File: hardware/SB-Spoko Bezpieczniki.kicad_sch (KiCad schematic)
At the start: 17 parts, among them IC1 STM32L4P5RET6, SW1 RESET, Y1 THE_CLOCK

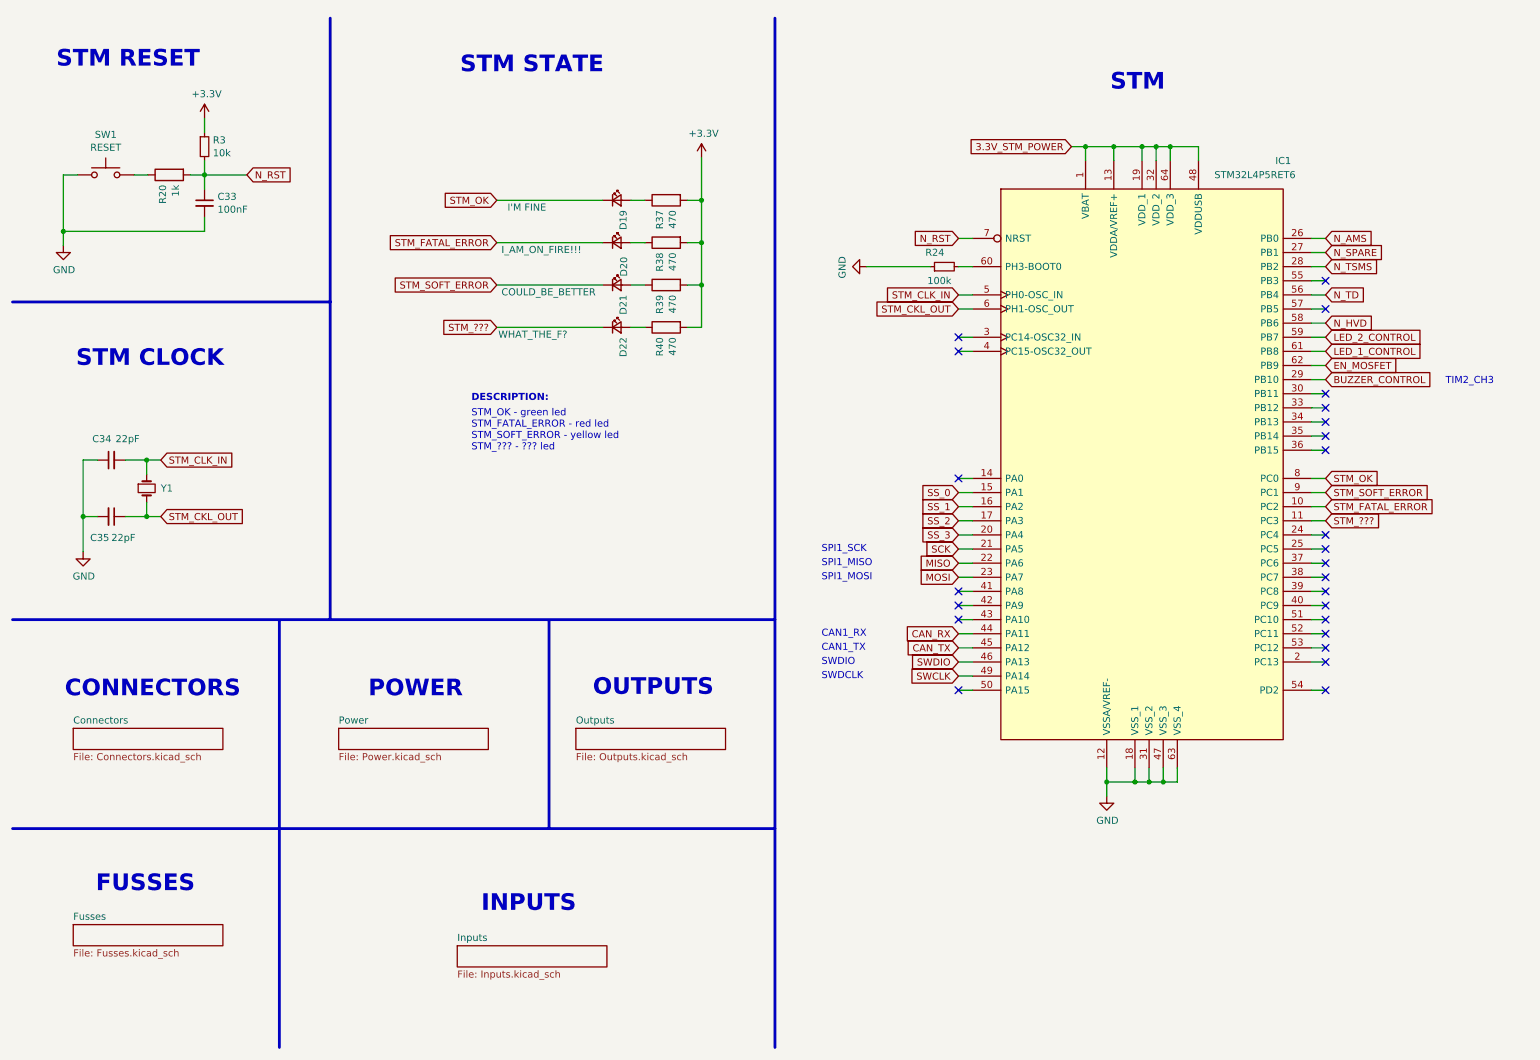
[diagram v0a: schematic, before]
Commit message: changed clock and 5v converter coils, footprints rearrange commponets to fit the need now the board connector is vertical not horizontal relative to the pcb's longest side
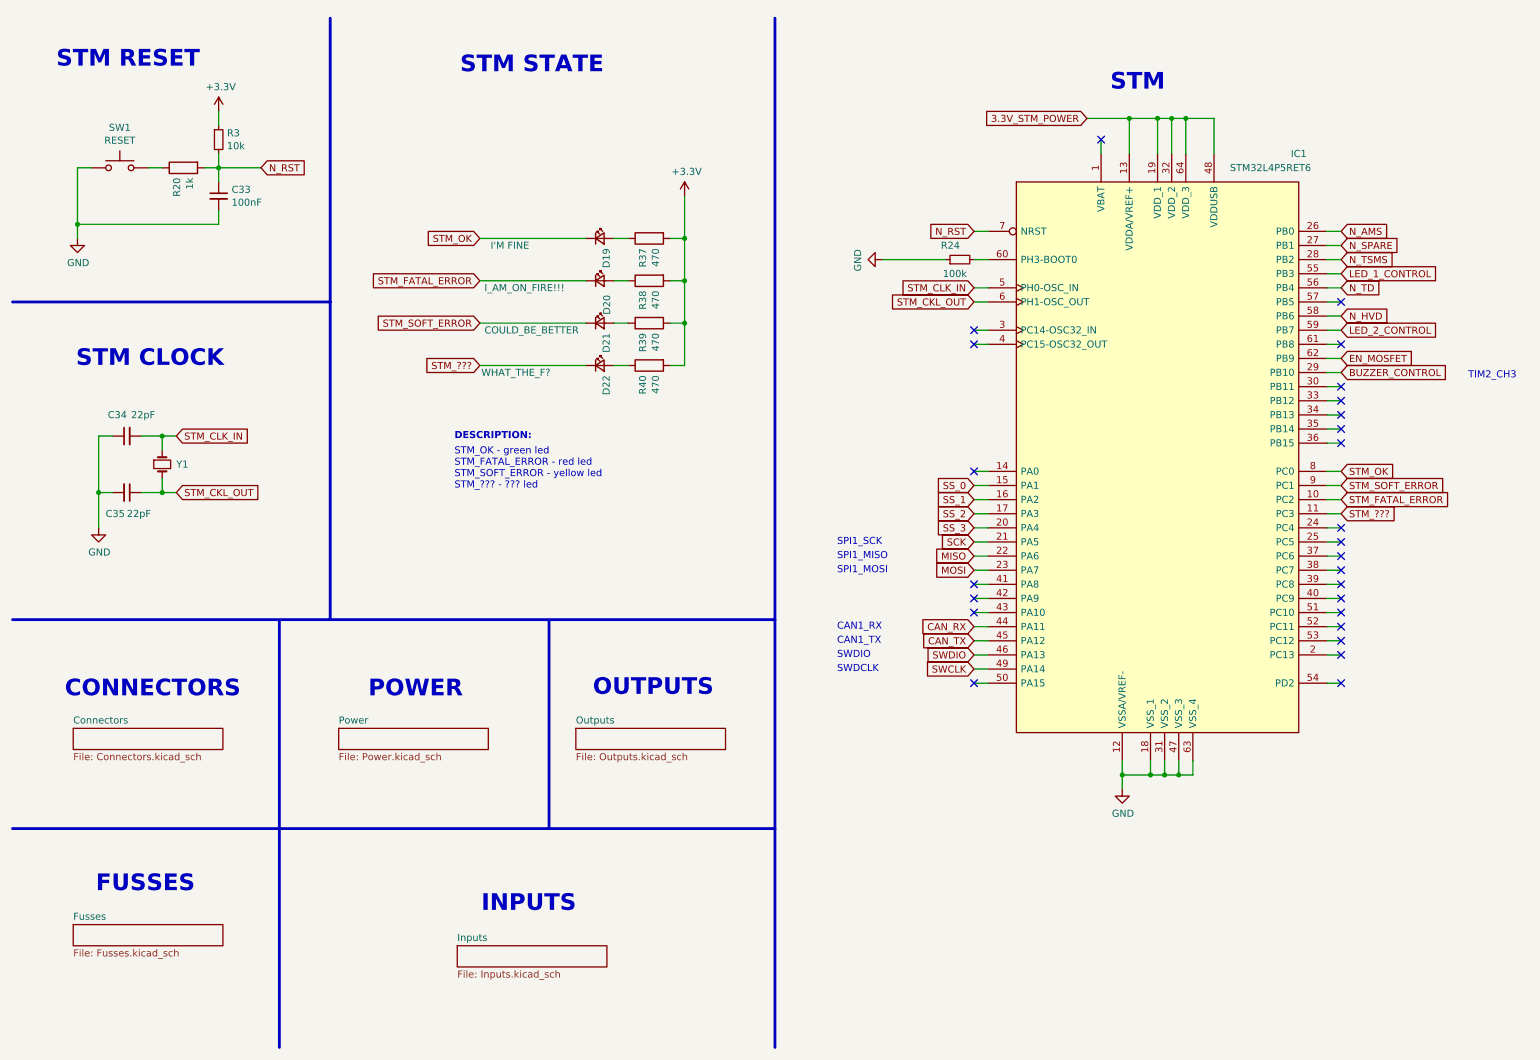
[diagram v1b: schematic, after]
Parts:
- Y1: footprint Crystal:Crystal_SMD_HC49-SD -> Crystal:Crystal_SMD_3225-4Pin_3.2x2.5mm
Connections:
- net 3.3V_STM_POWER: no longer IC1.1 (VBAT)
- net LED_1_CONTROL: now also IC1.55 (PB3); no longer IC1.61 (PB8)
- no-connect marks 25 -> 26
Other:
- moved on the sheet: C33, C34, C35, D19, D20, D21, D22, IC1, R20, R24, R3, R37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

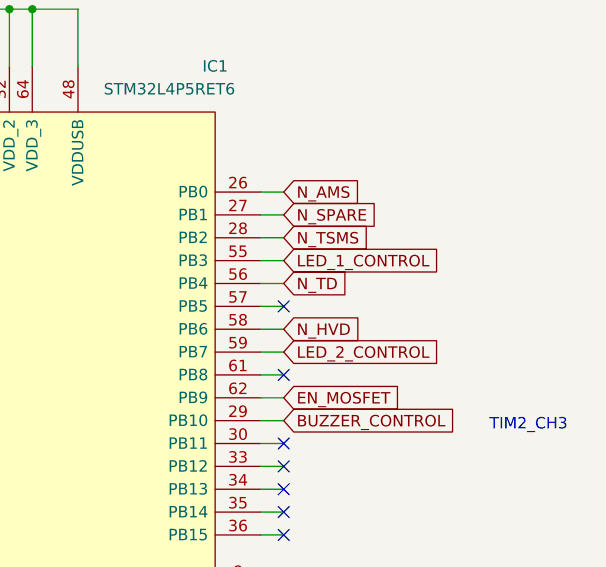
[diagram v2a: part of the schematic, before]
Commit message: added traceswo from pin 55 to progrmator
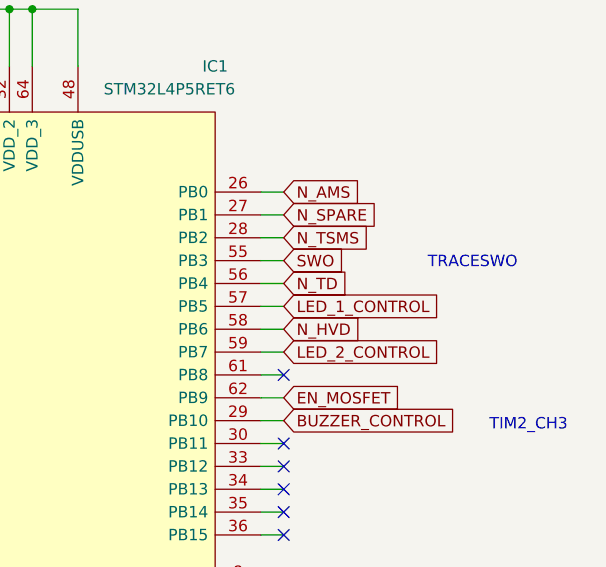
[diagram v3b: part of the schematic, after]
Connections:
- net LED_1_CONTROL: now also IC1.57 (PB5); no longer IC1.55 (PB3)
- new net SWO: IC1.55 (PB3)
- no-connect marks 26 -> 25
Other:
- note added: "TRACESWO"
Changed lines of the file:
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@@
   (no_connect (at 185.42 119.38))
   (no_connect (at 251.46 127))
-  (no_connect (at 251.46 63.5))
   (no_connect (at 251.46 88.9))
   (no_connect (at 251.46 106.68))
@@
     (stroke (width 0) (type default) (color 0 0 0 0))
   )
+  (wire (pts (xy 248.92 63.5) (xy 251.46 63.5))
+    (stroke (width 0) (type default) (color 0 0 0 0))
+  )
+  (wire (pts (xy 224.79 148.59) (xy 222.25 148.59))
+    (stroke (width 0) (type default) (color 0 0 0 0))
+  )
+  (wire (pts (xy 218.44 30.48) (xy 218.44 36.83))
+    (stroke (width 0) (type default) (color 0 0 0 0))
+  )
+  (wire (pts (xy 39.37 97.79) (xy 41.91 97.79))
+    (stroke (width 0) (type default) (color 0 0 0 0))
+  )
+  (wire (pts (xy 248.92 78.74) (xy 251.46 78.74))
+    (stroke (width 0) (type default) (color 0 0 0 0))
+  )
   (wire (pts (xy 248.92 58.42) (xy 251.46 58.42))
     (stroke (width 0) (type default) (color 0 0 0 0))
   )
-  (wire (pts (xy 224.79 148.59) (xy 222.25 148.59))
-    (stroke (width 0) (type default) (color 0 0 0 0))
-  )
-  (wire (pts (xy 218.44 30.48) (xy 218.44 36.83))
-    (stroke (width 0) (type default) (color 0 0 0 0))
-  )
-  (wire (pts (xy 39.37 97.79) (xy 41.91 97.79))
-    (stroke (width 0) (type default) (color 0 0 0 0))
-  )
-  (wire (pts (xy 248.92 78.74) (xy 251.46 78.74))
-    (stroke (width 0) (type default) (color 0 0 0 0))
-  )
-  (wire (pts (xy 248.92 63.5) (xy 251.46 63.5))
-    (stroke (width 0) (type default) (color 0 0 0 0))
-  )
   (wire (pts (xy 212.09 148.59) (xy 212.09 146.05))
     (stroke (width 0) (type default) (color 0 0 0 0))
@@
   )
   (text "SPI1_MOSI\n" (at 160.782 112.522 0)
+    (effects (font (size 1.27 1.27)) (justify left bottom))
+  )
+  (text "TRACESWO" (at 267.462 59.436 0)
     (effects (font (size 1.27 1.27)) (justify left bottom))
   )
@@
     )
   )
-  (global_label "LED_1_CONTROL" (shape input) (at 251.46 58.42 0) (fields_autoplaced)
-    (effects (font (size 1.27 1.27)) (justify left))
-    (property "Intersheet References" "${INTERSHEET_REFS}" (id 0) (at -24.13 -90.17 0)
+  (global_label "LED_1_CONTROL" (shape input) (at 251.46 63.5 0) (fields_autoplaced)
+    (effects (font (size 1.27 1.27)) (justify left))
+    (property "Intersheet References" "${INTERSHEET_REFS}" (id 0) (at -24.13 -85.09 0)
       (effects (font (size 1.27 1.27)) hide)
     )
@@
     )
   )
+  (global_label "SWO" (shape input) (at 251.46 58.42 0) (fields_autoplaced)
+    (effects (font (size 1.27 1.27)) (justify left))
+    (property "Intersheet References" "${INTERSHEET_REFS}" (id 0) (at 257.7756 58.3406 0)
+      (effects (font (size 1.27 1.27)) (justify left) hide)
+    )
+  )

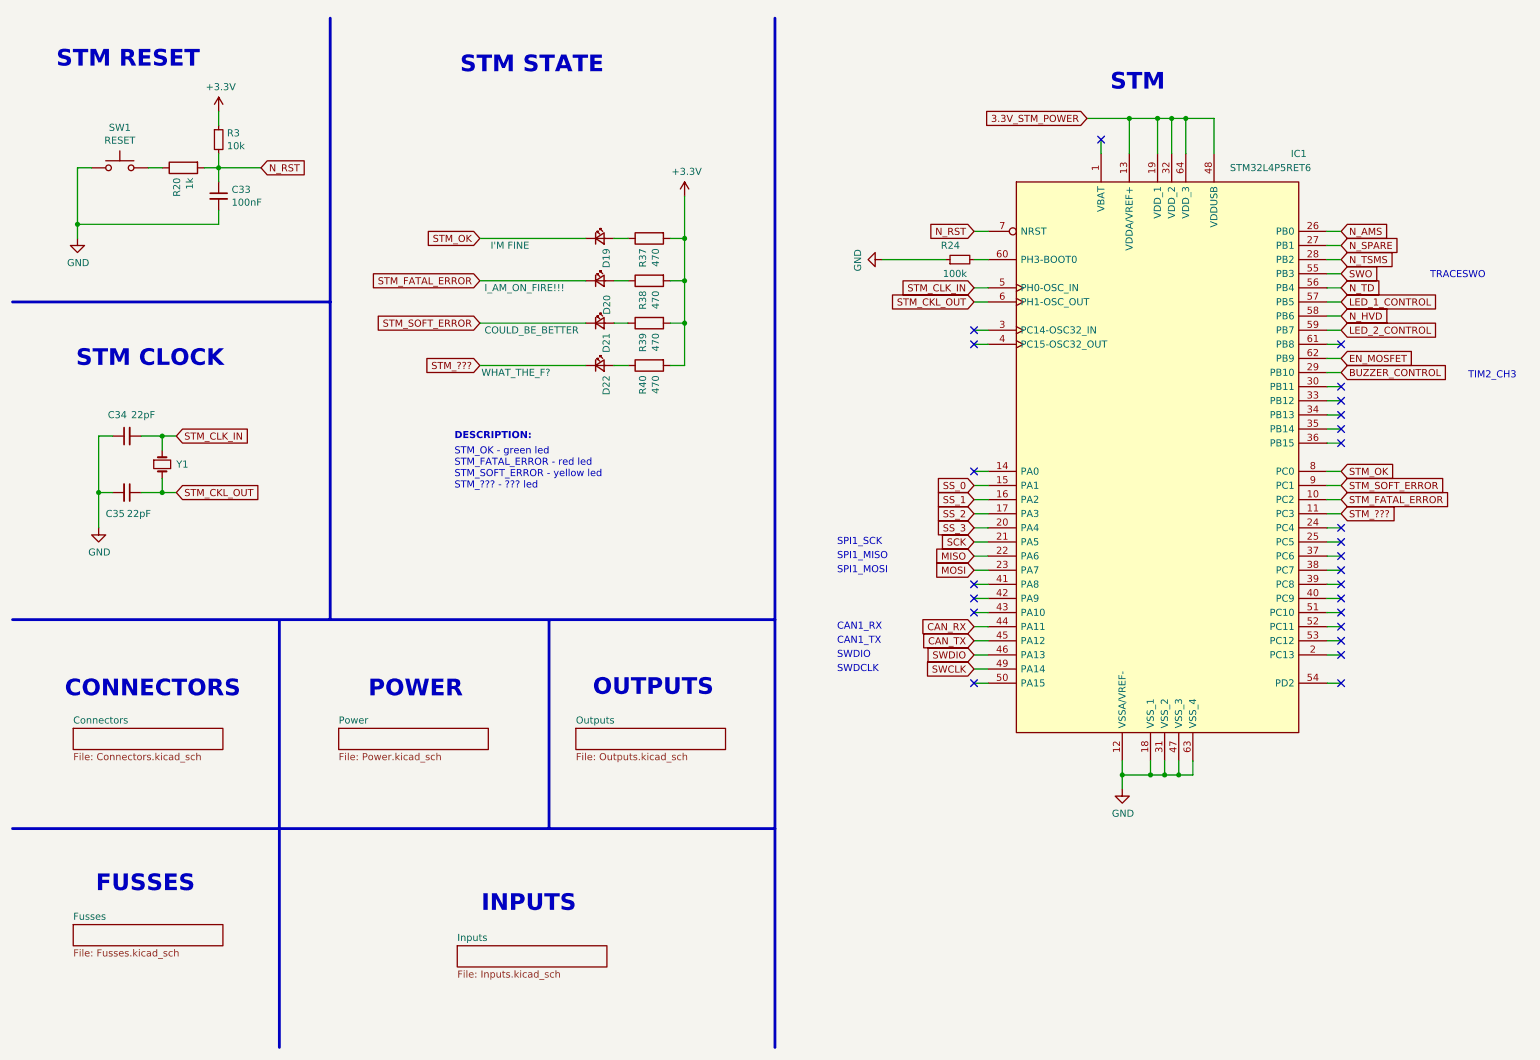
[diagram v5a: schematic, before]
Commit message: major schematic update, changed optocouplers for different, added new fuses for 5v supply for water and potentiometers and 24v supply for BSPD/ESB, updated autosport connector, and some other changes
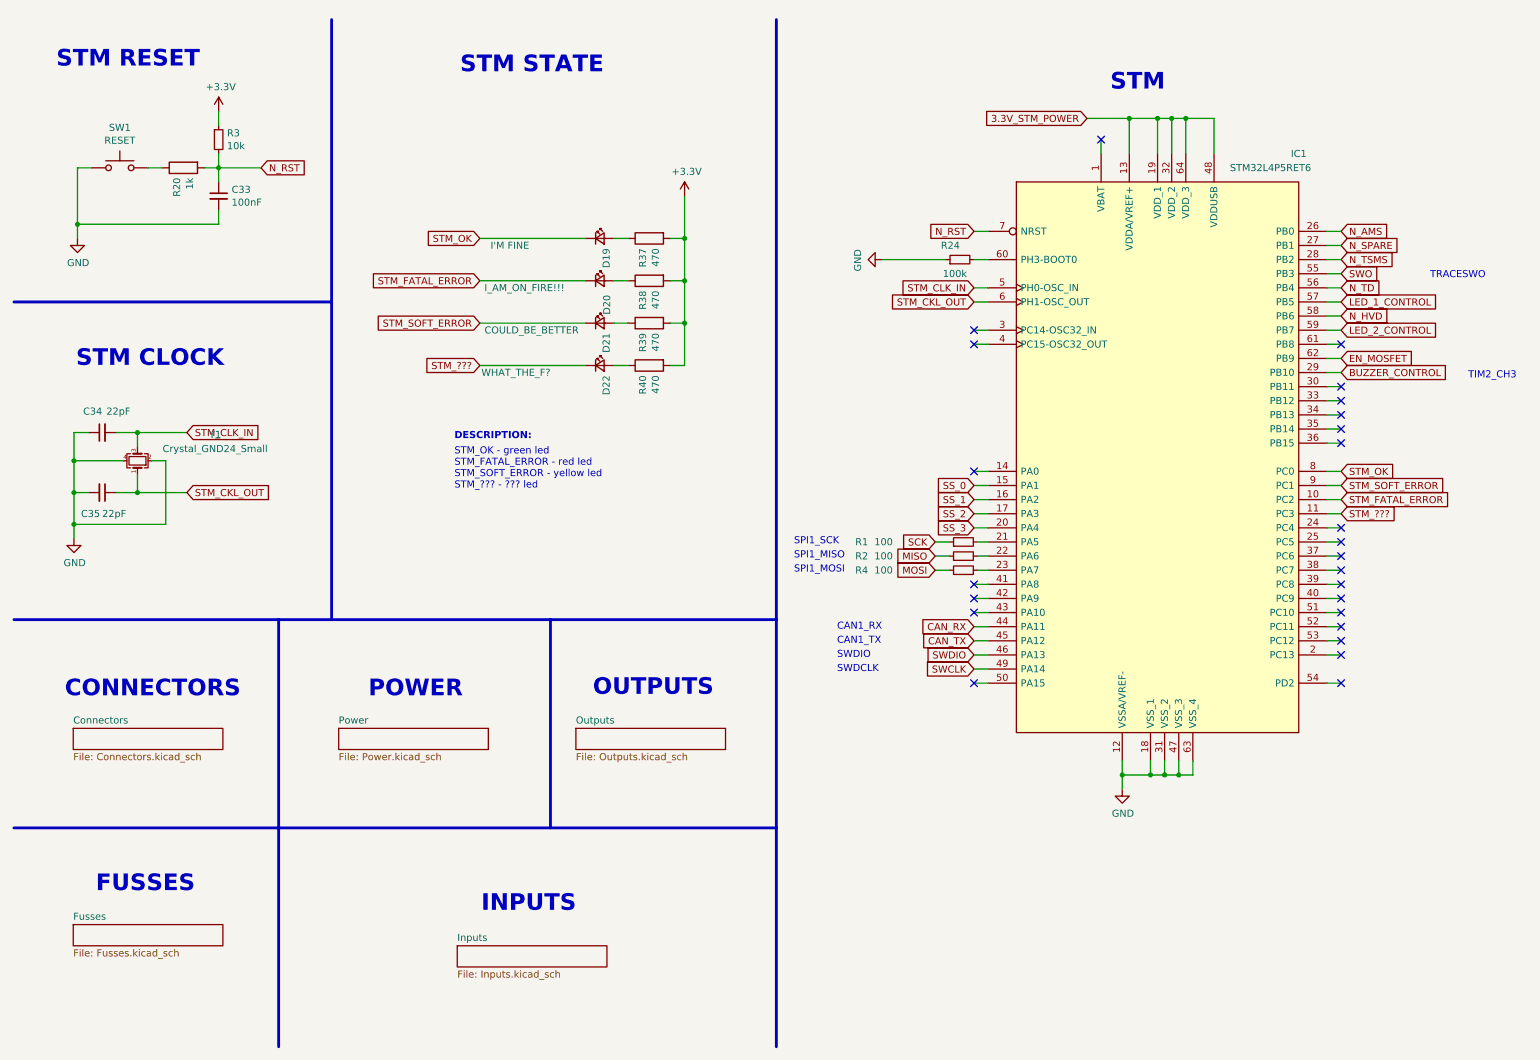
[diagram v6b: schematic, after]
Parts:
- removed Y1: THE_CLOCK, Crystal:Crystal_SMD_3225-4Pin_3.2x2.5mm, symbol Device:Crystal_Small
- added R1, R2, R4: 100, Resistor_SMD:R_0603_1608Metric, symbol Device:R_Small
- added Y1: Crystal_GND24_Small, Crystal:Crystal_SMD_3225-4Pin_3.2x2.5mm, symbol Device:Crystal_GND24_Small
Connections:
- net GND: now also Y1.2, Y1.4
- net MISO: now also R2.1; no longer IC1.22 (PA6)
- net MOSI: now also R4.1; no longer IC1.23 (PA7)
- net SCK: now also R1.1; no longer IC1.21 (PA5)
- net STM_CKL_OUT: now also Y1.1
- net STM_CLK_IN: now also Y1.3
- new net: IC1.21 (PA5), R1.2
- new net: IC1.22 (PA6), R2.2
- new net: IC1.23 (PA7), R4.2
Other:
- moved on the sheet: C34, C35

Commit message: changed some footprints for clarity, and made some progress on board
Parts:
- added R50, R51: 100, Resistor_SMD:R_0603_1608Metric, symbol Device:R_Small
- added R52: 0, Resistor_SMD:R_0603_1608Metric, symbol Device:R_Small
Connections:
- net +3V3: no longer R3.1
- net 3.3V_STM_POWER: now also R3.1; no longer IC1.13 (VDDA/VREF+)
- net BUZZER_CONTROL: now also R52.1; no longer IC1.29 (PB10)
- net CAN_RX: now also R50.1; no longer IC1.44 (PA11)
- net CAN_TX: now also R51.1; no longer IC1.45 (PA12)
- net SPARE_3_SENSE_SIG: now reaches IC1.2 (PC13)
- net BSPD/EBS_STATE: now reaches IC1.24 (PC4)
- net BSPD/EBS_IMON: now reaches IC1.25 (PC5)
- net DV_SENSE_SIG: now reaches IC1.37 (PC6)
- net FIREWALL_SENSE_SIG: now reaches IC1.38 (PC7)
- net HVD_SENSE_SIG: now reaches IC1.39 (PC8)
- net HV_SENSE_SIG: now reaches IC1.40 (PC9)
- net INVERTER_SENSE_SIG: now reaches IC1.51 (PC10)
- net SPARE_1_SENSE_SIG: now reaches IC1.52 (PC11)
- net SPARE_2_SENSE_SIG: now reaches IC1.53 (PC12)
- net EN_MOSFET: no longer names the net of IC1.62 (PB9)
- net N_AMS renamed WATER/POT_IMON
- net N_HVD: no longer names the net of IC1.58 (PB6)
- net N_SPARE renamed WATER/POT_STATE
- net N_TD: no longer names the net of IC1.56 (PB4)
- net N_TSMS renamed WATER/POT_ENABLE
- new net: IC1.29 (PB10), R52.2
- new net: IC1.44 (PA11), R50.2
- new net: IC1.45 (PA12), R51.2
- new net 3.3V_STM_REF+: IC1.13 (VDDA/VREF+)
- no-connect marks 25 -> 18
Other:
- note added: "ADC1 13"
- note added: "ADC1 14"
- note added: "ADC1 15"
- moved on the sheet: C33, IC1, R1, R2, R20, R24, R3, R4, SW1

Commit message: finished new wersion of the board
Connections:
- net DV_SENSE_SIG: now also IC1.53 (PC12); no longer IC1.37 (PC6)
- net FIREWALL_SENSE_SIG: now also IC1.52 (PC11); no longer IC1.38 (PC7)
- net HVD_SENSE_SIG: now also IC1.40 (PC9); no longer IC1.39 (PC8)
- net HV_SENSE_SIG: now also IC1.39 (PC8); no longer IC1.40 (PC9)
- net SPARE_1_SENSE_SIG: now also IC1.2 (PC13); no longer IC1.52 (PC11)
- net SPARE_2_SENSE_SIG: now also IC1.37 (PC6); no longer IC1.53 (PC12)
- net SPARE_3_SENSE_SIG: now also IC1.38 (PC7); no longer IC1.2 (PC13)
- net STM_???: now also IC1.8 (PC0); no longer IC1.11 (PC3)
- net STM_FATAL_ERROR: now also IC1.9 (PC1); no longer IC1.10 (PC2)
- net STM_OK: now also IC1.11 (PC3); no longer IC1.8 (PC0)
- net STM_SOFT_ERROR: now also IC1.10 (PC2); no longer IC1.9 (PC1)
- net WATER/POT_STATE: now also IC1.56 (PB4); no longer IC1.27 (PB1)
- net TSAL_IMON: now reaches IC1.14 (PA0)
- net TSAL_ENABLE: now reaches IC1.58 (PB6)
- new net TSAL_STATE: IC1.27 (PB1)
- no-connect marks 18 -> 15
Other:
- note added: "ADC1 16"
- note added: "ADC1 5"
